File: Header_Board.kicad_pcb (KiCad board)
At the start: 2 copper layers, 90.2 x 95.9 mm, 6 parts, among them P1 Socket_Strip_Straight_2x26_Pi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, P2 Socket_Strip_Straight_2x26_Pi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

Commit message: Add files via upload
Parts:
- added J1: Conn_Coaxial, Connectors:SMA_SMD_Jack_Straight, F.Cu at (95.5, 84.7)
- added J2: Conn_Coaxial, Connectors:SMA_SMD_Jack_Straight, F.Cu at (95.8, 138.7)
- added P3: CONN_02X30, Connectors_Samtec:MECF-30-01-NP-L-DV-WT_Socket, F.Cu at (127.0, 146.1)
- added U1: TAMP_1512GLN+, Project:TAMP-1512GLN+, F.Cu at (132.5, 105.9)
- added U10: TAMP_1512GLN+, Project:TAMP-1512GLN+, F.Cu at (123.6, 80.9)
- added U11: LAT, Project:LAT_1+, F.Cu at (93.0, 105.4)
- added U12: TAMP_1512GLN+, Project:TAMP-1512GLN+, F.Cu at (120.7, 137.4)
- added U13: LAT, Project:LAT_1+, F.Cu at (90.9, 110.7)
- added U14: LAT, Project:LAT_1+, F.Cu at (142.6, 85.3)
- added U15: LAT, Project:LAT_1+, F.Cu at (118.9, 123.2)
- added U16: CBP-1400E+, Project:CBP-1400E+, F.Cu at (95.0, 114.2)
- added U17: LAT, Project:LAT_1+, F.Cu at (117.0, 118.5)
- added U18: LAT, Project:LAT_1+, F.Cu at (114.9, 113.0)
- added U2: CBP-1400E+, Project:CBP-1400E+, F.Cu at (102.5, 86.5)
- added U3: LAT, Project:LAT_1+, F.Cu at (140.2, 111.9)
- added U4: LAT, Project:LAT_1+, F.Cu at (145.8, 111.8)
- added U5: LAT, Project:LAT_1+, F.Cu at (112.3, 101.5)
- added U6: LAT, Project:LAT_1+, F.Cu at (108.5, 103.1)
- added U7: LAT, Project:LAT_1+, F.Cu at (103.1, 101.5)
- added U8: CBP-1400E+, Project:CBP-1400E+, F.Cu at (144.8, 91.9)
- added U9: LAT, Project:LAT_1+, F.Cu at (98.2, 103.5)
- P1, P2: value Socket_Strip_Straight_2x26_Pitch2.54mm -> CONN_02X26
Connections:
- P1 pad 1: (no net) -> /GPIO0
- P1 pad 10: (no net) -> /GPIO7
- P1 pad 11: (no net) -> /GPIO8
- P1 pad 12: (no net) -> /GPIO9
- P1 pad 13: (no net) -> /GPIO10
- P1 pad 14: (no net) -> /GPIO11
- P1 pad 15: (no net) -> /GPIO12
- P1 pad 16: (no net) -> /GPIO13
- P1 pad 17: (no net) -> /RADIO_RX
- P1 pad 18: (no net) -> /RADIO_TX
- P1 pad 19: (no net) -> /12C2_SDA
- P1 pad 2: (no net) -> /GPIO1
- P1 pad 20: (no net) -> /I2C2_SCL
- P1 pad 21: (no net) -> /SYS_SPI_SCK
- P1 pad 22: (no net) -> /SYS_SPI_MISO
- P1 pad 23: (no net) -> /SYS_SPI_MOSI
- P1 pad 24: (no net) -> /SYS_SPI_NSS
- P1 pad 25: (no net) -> Net-(P1-Pad25)
- P1 pad 26: (no net) -> Net-(P1-Pad26)
- P1 pad 27: (no net) -> Net-(P1-Pad27)
- P1 pad 28: (no net) -> Net-(P1-Pad28)
- P1 pad 29: (no net) -> /SYS_RESET
- P1 pad 3: (no net) -> /GPIO2
- P1 pad 30: (no net) -> Net-(P1-Pad30)
- P1 pad 31: (no net) -> Net-(P1-Pad31)
- P1 pad 32: (no net) -> Net-(P1-Pad32)
- P1 pad 33: (no net) -> /SGPIO7
- P1 pad 34: (no net) -> /SGPIO8
- P1 pad 35: (no net) -> /SGPIO9
- P1 pad 36: (no net) -> /SGPIO10
- P1 pad 37: (no net) -> /SGPIO11
- P1 pad 38: (no net) -> /SGPIO12
- P1 pad 39: (no net) -> /SGPIO13
- P1 pad 4: (no net) -> /GPIO3
- P1 pad 40: (no net) -> /SGPIO14
- P1 pad 41: (no net) -> /SYS_SDA
- P1 pad 42: (no net) -> Net-(P1-Pad42)
- P1 pad 43: (no net) -> /SYS_SCL
- P1 pad 44: (no net) -> Net-(P1-Pad44)
- P1 pad 45: (no net) -> Net-(P1-Pad45)
- P1 pad 46: (no net) -> Net-(P1-Pad46)
- P1 pad 47: (no net) -> /NBUFEN_PRI
- P1 pad 48: (no net) -> /NBUFEN_SEC
- P1 pad 49: (no net) -> /I2C2_SDA
- P1 pad 5: (no net) -> /RADIO_TR
- P1 pad 50: (no net) -> /SGPIO5
- P1 pad 51: (no net) -> /I2C2_SCL
- P1 pad 52: (no net) -> /SGPIO6
- P1 pad 6: (no net) -> /RADIO_RR
- P1 pad 7: (no net) -> /GPIO4
- P1 pad 8: (no net) -> /GPIO5
- P1 pad 9: (no net) -> /GPIO6
- P2 pad 1: (no net) -> /SGPIO0
- P2 pad 10: (no net) -> Net-(P2-Pad10)
- P2 pad 11: (no net) -> Net-(P2-Pad11)
- P2 pad 12: (no net) -> Net-(P2-Pad12)
- P2 pad 13: (no net) -> Net-(P2-Pad13)
- P2 pad 14: (no net) -> GND
- P2 pad 15: (no net) -> Net-(P2-Pad15)
- P2 pad 16: (no net) -> Net-(P2-Pad16)
- P2 pad 17: (no net) -> GND
- P2 pad 18: (no net) -> Net-(P2-Pad18)
- P2 pad 19: (no net) -> Net-(P2-Pad19)
- P2 pad 2: (no net) -> /SGPIO1
- P2 pad 20: (no net) -> Net-(P2-Pad20)
- P2 pad 21: (no net) -> GND
- P2 pad 22: (no net) -> GND
- P2 pad 23: (no net) -> Net-(P2-Pad23)
- P2 pad 24: (no net) -> Net-(P2-Pad24)
- P2 pad 25: (no net) -> +5V
- P2 pad 26: (no net) -> +5V
- P2 pad 27: (no net) -> +3V3
- P2 pad 28: (no net) -> +3V3
- P2 pad 29: (no net) -> GND
- P2 pad 3: (no net) -> /SGPIO2
- P2 pad 30: (no net) -> GND
- P2 pad 31: (no net) -> Net-(P2-Pad31)
- P2 pad 32: (no net) -> GND
- P2 pad 33: (no net) -> Net-(P2-Pad33)
- P2 pad 34: (no net) -> Net-(P2-Pad34)
- P2 pad 35: (no net) -> Net-(P2-Pad35)
- P2 pad 36: (no net) -> Net-(P2-Pad36)
- P2 pad 37: (no net) -> Net-(P2-Pad37)
- P2 pad 38: (no net) -> Net-(P2-Pad38)
- P2 pad 39: (no net) -> Net-(P2-Pad39)
- P2 pad 4: (no net) -> /SGPIO3
- P2 pad 40: (no net) -> Net-(P2-Pad40)
- P2 pad 41: (no net) -> Net-(P2-Pad41)
- P2 pad 42: (no net) -> Net-(P2-Pad42)
- P2 pad 43: (no net) -> Net-(P2-Pad43)
- P2 pad 44: (no net) -> Net-(P2-Pad44)
- P2 pad 45: (no net) -> Net-(P2-Pad45)
- P2 pad 46: (no net) -> Net-(P2-Pad46)
- P2 pad 47: (no net) -> GND
- P2 pad 48: (no net) -> GND
- P2 pad 49: (no net) -> /SPI2_NSS
- P2 pad 5: (no net) -> /I2C3_SDA
- P2 pad 50: (no net) -> /SPI2_SCK
- P2 pad 51: (no net) -> /SPI2_MISO
- P2 pad 52: (no net) -> /SPI2_MOSI
- P2 pad 6: (no net) -> /I2C3_SCL
- P2 pad 7: (no net) -> /SGPIO4
- P2 pad 8: (no net) -> Net-(P2-Pad8)
- P2 pad 9: (no net) -> GND
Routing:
- net GND: track 0.00 -> 574.2 mm, vias 0 -> 55
- net Net-(U1-Pad2): track 0.00 -> 16.4 mm
- net Net-(J2-Pad1): track 0.00 -> 13.1 mm
- net Net-(U12-Pad2): track 0.00 -> 13.1 mm
- net Net-(J1-Pad1): track 0.00 -> 8.74 mm
- net Net-(U14-Pad2): track 0.00 -> 7.46 mm
- net Net-(U10-Pad2): track 0.00 -> 4.61 mm
- net Net-(U3-Pad4): track 0.00 -> 4.11 mm
- net Net-(U1-Pad7): track 0.00 -> 3.83 mm
- net Net-(U10-Pad7): track 0.00 -> 3.70 mm
- net Net-(U13-Pad2): track 0.00 -> 3.50 mm
- net Net-(U17-Pad4): track 0.00 -> 3.30 mm
- net Net-(U11-Pad4): track 0.00 -> 3.00 mm
- net Net-(U16-Pad11): track 0.00 -> 2.91 mm
- net Net-(U4-Pad4): track 0.00 -> 2.82 mm
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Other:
- copper layers 2 -> 4
- net class RF_Track added: clearance 0.2, trace_width 1.84, via_dia 0.6, via_drill 0.4

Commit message: Progress on board layout
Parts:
- added G***: LOGO, breakoutBoard:Cysized, F.Cu at (153.5, 134.4)
- moved P3 56.7 mm to (87.9, 105.0), turned to 90 degrees
- moved U4 15.4 mm to (161.2, 111.1)
- moved J2 15.4 mm to (111.1, 138.0)
- moved U11 15.4 mm to (108.3, 104.8)
- moved U13 15.4 mm to (106.3, 110.1)
- moved U15 15.4 mm to (134.2, 122.6)
- moved U16 15.4 mm to (110.4, 113.5)
- moved U17 15.4 mm to (132.3, 117.9)
- moved U5 15.4 mm to (127.6, 100.8)
- moved U6 15.4 mm to (123.8, 102.5)
- moved U7 15.4 mm to (118.5, 100.8)
- moved J1 15.4 mm to (110.9, 84.1)
- moved U1 15.4 mm to (147.8, 105.3)
- moved U10 15.4 mm to (138.9, 80.3)
- moved U12 15.4 mm to (136.0, 136.8)
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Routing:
- net GND: track 574.2 -> 23.7 mm, vias 55 -> 0
- added copper zone on F.Cu, net GND
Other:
- board text added: "CySat 1 - RF Board"

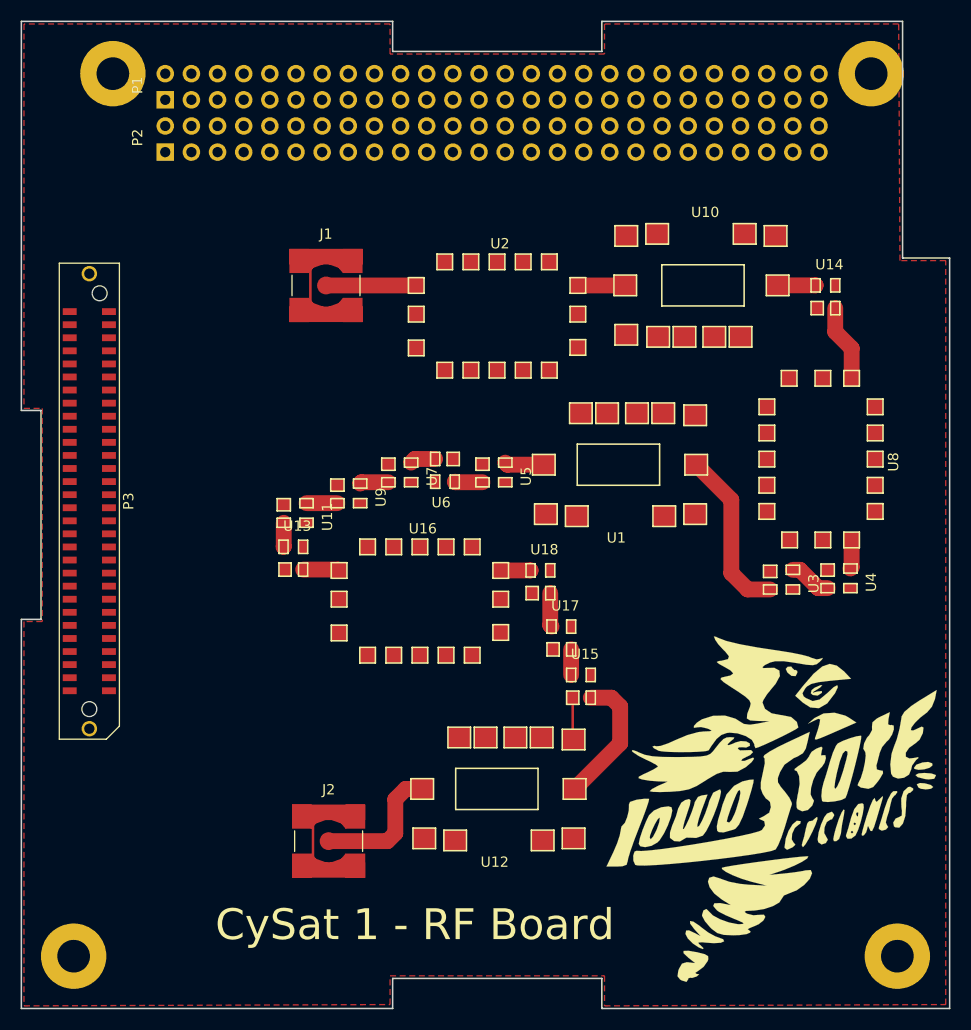
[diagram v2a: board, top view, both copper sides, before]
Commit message: Tentative cardedge routing and gerbers
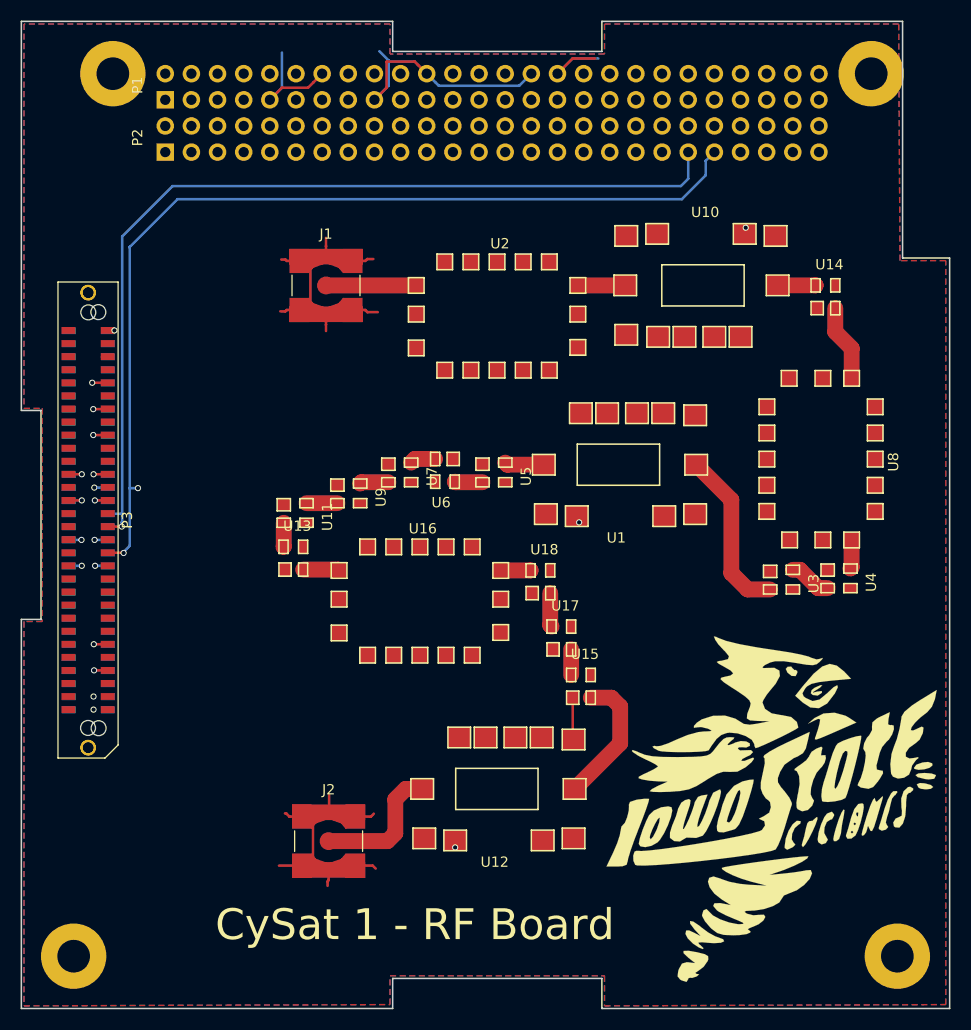
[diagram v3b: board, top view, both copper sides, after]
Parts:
- added G***: LOGO, Radiometer-RF-Board:eye, B.Cu at (129.0, 111.8)
- added P3: CONN_02X30, Connectors_Samtec:MECF-30-01-NP-L-DV-WT_Socket, B.Cu at (87.8, 106.9)
- moved P3 1.83 mm to (87.8, 106.9)
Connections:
- P1 pad 1: /GPIO0 -> /SGPIO0
- P1 pad 10: /GPIO7 -> Net-(P1-Pad10)
- P1 pad 11: /GPIO8 -> Net-(P1-Pad11)
- P1 pad 12: /GPIO9 -> Net-(P1-Pad12)
- P1 pad 13: /GPIO10 -> Net-(P1-Pad13)
- P1 pad 14: /GPIO11 -> GND
- P1 pad 15: /GPIO12 -> Net-(P1-Pad15)
- P1 pad 16: /GPIO13 -> Net-(P1-Pad16)
- P1 pad 17: /RADIO_RX -> GND
- P1 pad 18: /RADIO_TX -> Net-(P1-Pad18)
- P1 pad 19: /12C2_SDA -> Net-(P1-Pad19)
- P1 pad 2: /GPIO1 -> /SGPIO1
- P1 pad 20: /I2C2_SCL -> Net-(P1-Pad20)
- P1 pad 21: /SYS_SPI_SCK -> GND
- P1 pad 22: /SYS_SPI_MISO -> GND
- P1 pad 23: /SYS_SPI_MOSI -> Net-(P1-Pad23)
- P1 pad 24: /SYS_SPI_NSS -> Net-(P1-Pad24)
- P1 pad 25: Net-(P1-Pad25) -> +5V
- P1 pad 26: Net-(P1-Pad26) -> +5V
- P1 pad 29: /SYS_RESET -> GND
- P1 pad 3: /GPIO2 -> /SGPIO2
- P1 pad 30: Net-(P1-Pad30) -> GND
- P1 pad 32: Net-(P1-Pad32) -> GND
- P1 pad 33: /SGPIO7 -> Net-(P1-Pad33)
- P1 pad 34: /SGPIO8 -> Net-(P1-Pad34)
- P1 pad 35: /SGPIO9 -> Net-(P1-Pad35)
- P1 pad 36: /SGPIO10 -> Net-(P1-Pad36)
- P1 pad 37: /SGPIO11 -> Net-(P1-Pad37)
- P1 pad 38: /SGPIO12 -> Net-(P1-Pad38)
- P1 pad 39: /SGPIO13 -> Net-(P1-Pad39)
- P1 pad 4: /GPIO3 -> /SGPIO3
- P1 pad 40: /SGPIO14 -> Net-(P1-Pad40)
- P1 pad 41: /SYS_SDA -> Net-(P1-Pad41)
- P1 pad 43: /SYS_SCL -> Net-(P1-Pad43)
- P1 pad 47: /NBUFEN_PRI -> GND
- P1 pad 48: /NBUFEN_SEC -> GND
- P1 pad 49: /I2C2_SDA -> /SPI2_NSS
- P1 pad 5: /RADIO_TR -> /I2C3_SDA
- P1 pad 50: /SGPIO5 -> /SPI2_SCK
- P1 pad 51: /I2C2_SCL -> /SPI2_MISO
- P1 pad 52: /SGPIO6 -> /SPI2_MOSI
- P1 pad 6: /RADIO_RR -> /I2C3_SCL
- P1 pad 7: /GPIO4 -> /SGPIO4
- P1 pad 8: /GPIO5 -> Net-(P1-Pad8)
- P1 pad 9: /GPIO6 -> GND
- P2 pad 1: /SGPIO0 -> /GPIO0
- P2 pad 10: Net-(P2-Pad10) -> /GPIO7
- P2 pad 11: Net-(P2-Pad11) -> /GPIO8
- P2 pad 12: Net-(P2-Pad12) -> /GPIO9
- P2 pad 13: Net-(P2-Pad13) -> /GPIO10
- P2 pad 14: GND -> /GPIO11
- P2 pad 15: Net-(P2-Pad15) -> /GPIO12
- P2 pad 16: Net-(P2-Pad16) -> /GPIO13
- P2 pad 17: GND -> /RADIO_RX
- P2 pad 18: Net-(P2-Pad18) -> /RADIO_TX
- P2 pad 19: Net-(P2-Pad19) -> /12C2_SDA
- P2 pad 2: /SGPIO1 -> /GPIO1
- P2 pad 20: Net-(P2-Pad20) -> /I2C2_SCL
- P2 pad 21: GND -> /SYS_SPI_SCK
- P2 pad 22: GND -> /SYS_SPI_MISO
- P2 pad 23: Net-(P2-Pad23) -> /SYS_SPI_MOSI
- P2 pad 24: Net-(P2-Pad24) -> /SYS_SPI_NSS
- P2 pad 25: +5V -> Net-(P2-Pad25)
- P2 pad 26: +5V -> Net-(P2-Pad26)
- P2 pad 27: +3V3 -> Net-(P2-Pad27)
- P2 pad 28: +3V3 -> Net-(P2-Pad28)
- P2 pad 29: GND -> /SYS_RESET
- P2 pad 3: /SGPIO2 -> /GPIO2
- P2 pad 30: GND -> Net-(P2-Pad30)
- P2 pad 32: GND -> Net-(P2-Pad32)
- P2 pad 33: Net-(P2-Pad33) -> /SGPIO7
- P2 pad 34: Net-(P2-Pad34) -> /SGPIO8
- P2 pad 35: Net-(P2-Pad35) -> /SGPIO9
- P2 pad 36: Net-(P2-Pad36) -> /SGPIO10
- P2 pad 37: Net-(P2-Pad37) -> /SGPIO11
- P2 pad 38: Net-(P2-Pad38) -> /SGPIO12
- P2 pad 39: Net-(P2-Pad39) -> /SGPIO13
- P2 pad 4: /SGPIO3 -> /GPIO3
- P2 pad 40: Net-(P2-Pad40) -> /SGPIO14
- P2 pad 41: Net-(P2-Pad41) -> /SYS_SDA
- P2 pad 43: Net-(P2-Pad43) -> /SYS_SCL
- P2 pad 47: GND -> /NBUFEN_PRI
- P2 pad 48: GND -> /NBUFEN_SEC
- P2 pad 49: /SPI2_NSS -> Net-(P2-Pad49)
- P2 pad 5: /I2C3_SDA -> /RADIO_TR
- P2 pad 50: /SPI2_SCK -> /SGPIO5
- P2 pad 51: /SPI2_MISO -> Net-(P2-Pad51)
- P2 pad 52: /SPI2_MOSI -> /SGPIO6
- P2 pad 6: /I2C3_SCL -> /RADIO_RR
- P2 pad 7: /SGPIO4 -> /GPIO4
- P2 pad 8: Net-(P2-Pad8) -> /GPIO5
- P2 pad 9: GND -> /GPIO6
- P3 pad 10: /SYS_SDA -> Net-(P3-Pad10)
- P3 pad 11: +3V3 -> GND
- P3 pad 13: GND -> Net-(P3-Pad13)
- P3 pad 14: +3V3 -> Net-(P3-Pad14)
- P3 pad 15: /SPI2_MISO -> GND
- P3 pad 17: GND -> Net-(P3-Pad17)
- P3 pad 18: /SPI2_MOSI -> Net-(P3-Pad18)
- P3 pad 19: /SPI2_SCK -> GND
- P3 pad 2: +3V3 -> GND
- P3 pad 24: /SGPIO_0 -> GND
- P3 pad 25: /SGPIO_1 -> /SYS_SCL
- P3 pad 26: GND -> Net-(P3-Pad26)
- P3 pad 28: /SGPIO_2 -> GND
- P3 pad 29: /SGPIO_3 -> /SYS_SDA
- P3 pad 3: +5V -> GND
- P3 pad 30: GND -> Net-(P3-Pad30)
- P3 pad 32: /SPGIO_4 -> GND
- P3 pad 33: +3V3 -> +5V
- P3 pad 34: GND -> +5V
- P3 pad 36: +3V3 -> GND
- P3 pad 37: /SYS_SPI_MISO -> +5V
- P3 pad 38: GND -> +5V
- P3 pad 40: /SYS_SPI_MOSI -> GND
- P3 pad 41: /SYS_SPI_SCK -> Net-(P3-Pad41)
- P3 pad 42: GND -> Net-(P3-Pad42)
- P3 pad 44: /GPIO_7 -> GND
- P3 pad 45: /GPIO_8 -> Net-(P3-Pad45)
- P3 pad 46: GND -> Net-(P3-Pad46)
- P3 pad 48: /GPIO_9 -> GND
- P3 pad 49: /GPIO_10 -> Net-(P3-Pad49)
- P3 pad 5: GND -> Net-(P3-Pad5)
- P3 pad 50: GND -> Net-(P3-Pad50)
- P3 pad 52: /GPIO_11 -> GND
- P3 pad 53: +3V3 -> Net-(P3-Pad53)
- P3 pad 54: GND -> Net-(P3-Pad54)
- P3 pad 56: +3V3 -> GND
- P3 pad 57: +5V -> Net-(P3-Pad57)
- P3 pad 58: GND -> Net-(P3-Pad58)
- P3 pad 6: +12V -> Net-(P3-Pad6)
- P3 pad 60: +12V -> GND
- P3 pad 7: /SYS_SCL -> GND
- P3 pad 9: GND -> Net-(P3-Pad9)
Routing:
- net /SYS_SCL: track 0.00 -> 99.4 mm, vias 0 -> 3
- net /SYS_SDA: track 0.00 -> 90.9 mm, vias 0 -> 1
- net GND: track 23.7 -> 105.6 mm, vias 0 -> 8
- net +5V: track 1.48 -> 28.4 mm, vias 0 -> 11
- net Net-(P2-Pad25): track 0.00 -> 0.50 mm
- added copper zone on In1.Cu, net +5V
- added copper zone on B.Cu, net GND

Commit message: Fixed soldermask
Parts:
- moved G*** 52.6 mm to (181.6, 111.1)

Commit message: Moved routing
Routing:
- net /SYS_SDA: track 90.9 -> 100.7 mm
- net /SYS_SCL: track 99.4 -> 96.0 mm
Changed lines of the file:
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@@
     (thickness 1.6)
     (drawings 19)
-    (tracks 193)
+    (tracks 196)
     (zones 0)
     (modules 30)
@@
   (segment (start 89.662 107.4928) (end 91.0336 107.4928) (width 0.25) (layer F.Cu) (net 37))
   (segment (start 91.0336 107.4928) (end 91.0336 107.068536) (width 0.25) (layer B.Cu) (net 37))
-  (segment (start 91.074401 79.308799) (end 95.9612 74.422) (width 0.25) (layer B.Cu) (net 37))
   (segment (start 91.0336 107.068536) (end 91.074401 107.027735) (width 0.25) (layer B.Cu) (net 37))
-  (segment (start 146.057081 73.703719) (end 146.057081 71.120935) (width 0.25) (layer B.Cu) (net 37))
-  (segment (start 95.9612 74.422) (end 145.3388 74.422) (width 0.25) (layer B.Cu) (net 37))
-  (segment (start 145.3388 74.422) (end 146.057081 73.703719) (width 0.25) (layer B.Cu) (net 37))
   (segment (start 90.998201 106.2482) (end 89.6874 106.2482) (width 0.25) (layer B.Cu) (net 37))
   (segment (start 91.074401 106.3244) (end 90.998201 106.2482) (width 0.25) (layer B.Cu) (net 37))
-  (segment (start 91.074401 106.3244) (end 91.074401 79.308799) (width 0.25) (layer B.Cu) (net 37))
   (segment (start 91.074401 107.027735) (end 91.074401 106.3244) (width 0.25) (layer B.Cu) (net 37))
+  (segment (start 91.0336 107.4928) (end 91.8972 107.4928) (width 0.25) (layer In2.Cu) (net 37))
+  (segment (start 87.772401 104.652799) (end 83.82 100.700398) (width 0.25) (layer In2.Cu) (net 37))
+  (segment (start 87.772401 105.232803) (end 87.772401 104.652799) (width 0.25) (layer In2.Cu) (net 37))
+  (segment (start 91.0336 107.4928) (end 90.032398 107.4928) (width 0.25) (layer In2.Cu) (net 37))
+  (segment (start 90.032398 107.4928) (end 87.772401 105.232803) (width 0.25) (layer In2.Cu) (net 37))
+  (segment (start 83.82 100.700398) (end 83.82 81.915) (width 0.25) (layer In2.Cu) (net 37))
+  (segment (start 144.88208 72.295936) (end 145.207082 71.970934) (width 0.25) (layer In2.Cu) (net 37))
+  (segment (start 93.439064 72.295936) (end 144.88208 72.295936) (width 0.25) (layer In2.Cu) (net 37))
+  (segment (start 145.207082 71.970934) (end 146.057081 71.120935) (width 0.25) (layer In2.Cu) (net 37))
+  (segment (start 83.82 81.915) (end 93.439064 72.295936) (width 0.25) (layer In2.Cu) (net 37))
   (via (at 88.3666 103.7082) (size 0.6) (drill 0.4) (layers F.Cu B.Cu) (net 39))
   (via (at 92.6084 103.759) (size 0.6) (drill 0.4) (layers F.Cu B.Cu) (net 39))
   (via (at 91.2114 110.0582) (size 0.6) (drill 0.4) (layers F.Cu B.Cu) (net 39))
-  (segment (start 147.747082 71.970934) (end 147.747082 73.385318) (width 0.25) (layer B.Cu) (net 39))
-  (segment (start 148.597081 71.120935) (end 147.747082 71.970934) (width 0.25) (layer B.Cu) (net 39))
-  (segment (start 147.747082 73.385318) (end 145.4404 75.692) (width 0.25) (layer B.Cu) (net 39))
-  (segment (start 145.4404 75.692) (end 96.4438 75.692) (width 0.25) (layer B.Cu) (net 39))
-  (segment (start 96.4438 75.692) (end 91.7956 80.3402) (width 0.25) (layer B.Cu) (net 39))
   (segment (start 91.7956 109.3724) (end 91.1098 110.0582) (width 0.25) (layer B.Cu) (net 39))
   (segment (start 91.186 110.0328) (end 91.2114 110.0582) (width 0.25) (layer F.Cu) (net 39))
@@
   (segment (start 89.6874 103.7082) (end 88.3666 103.7082) (width 0.25) (layer B.Cu) (net 39))
   (segment (start 92.6084 103.759) (end 91.7956 103.759) (width 0.25) (layer B.Cu) (net 39))
-  (segment (start 91.7956 80.3402) (end 91.7956 103.759) (width 0.25) (layer B.Cu) (net 39))
   (segment (start 91.7956 103.759) (end 91.7956 109.3724) (width 0.25) (layer B.Cu) (net 39))
   (segment (start 88.4174 103.759) (end 88.3666 103.7082) (width 0.25) (layer In2.Cu) (net 39))
   (segment (start 92.6084 103.759) (end 88.4174 103.759) (width 0.25) (layer In2.Cu) (net 39))
+  (segment (start 92.6084 103.759) (end 92.6084 83.2866) (width 0.25) (layer In2.Cu) (net 39))
+  (segment (start 92.6084 83.2866) (end 102.87 73.025) (width 0.25) (layer In2.Cu) (net 39))
+  (segment (start 146.693016 73.025) (end 148.597081 71.120935) (width 0.25) (layer In2.Cu) (net 39))
+  (segment (start 102.87 73.025) (end 146.693016 73.025) (width 0.25) (layer In2.Cu) (net 39))
   (via (at 88.3158 118.9228) (size 0.6) (drill 0.4) (layers F.Cu B.Cu) (net 54))
   (via (at 88.3412 121.4628) (size 0.6) (drill 0.4) (layers F.Cu B.Cu) (net 54))
